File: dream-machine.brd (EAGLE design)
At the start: 17.8 x 21.6 mm, 8 parts, among them J1 AVR_SPI_PRG_62X3_LOCK, SW1 Now, U1 ATTINY13SOIC

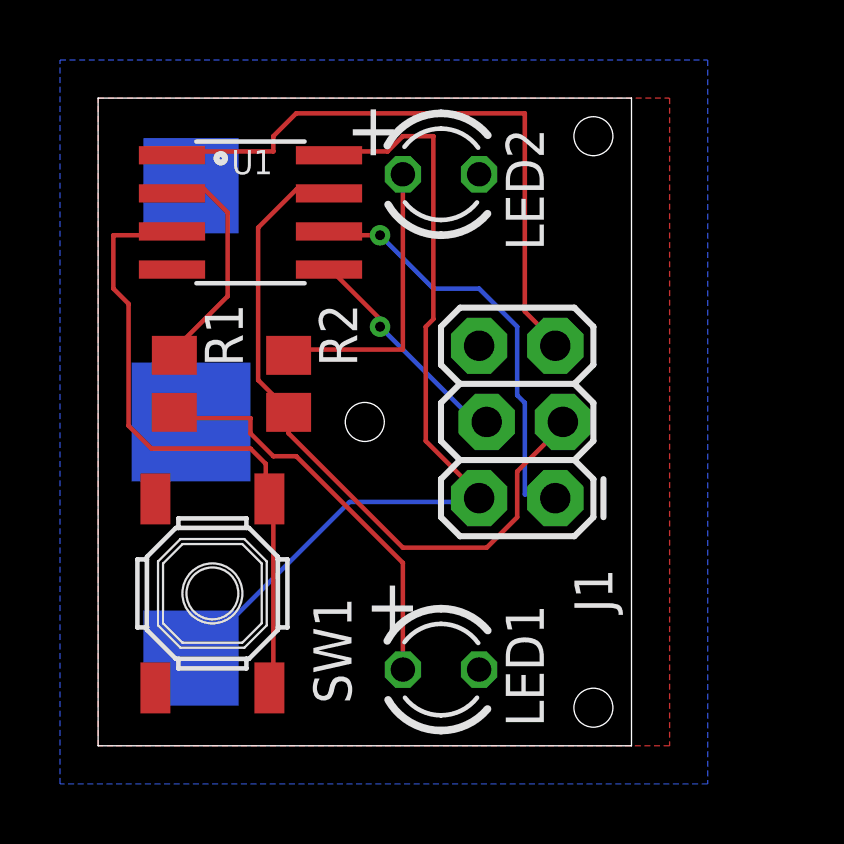
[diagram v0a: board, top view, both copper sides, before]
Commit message: Added power jumper. Fixed orientation of battery holder.
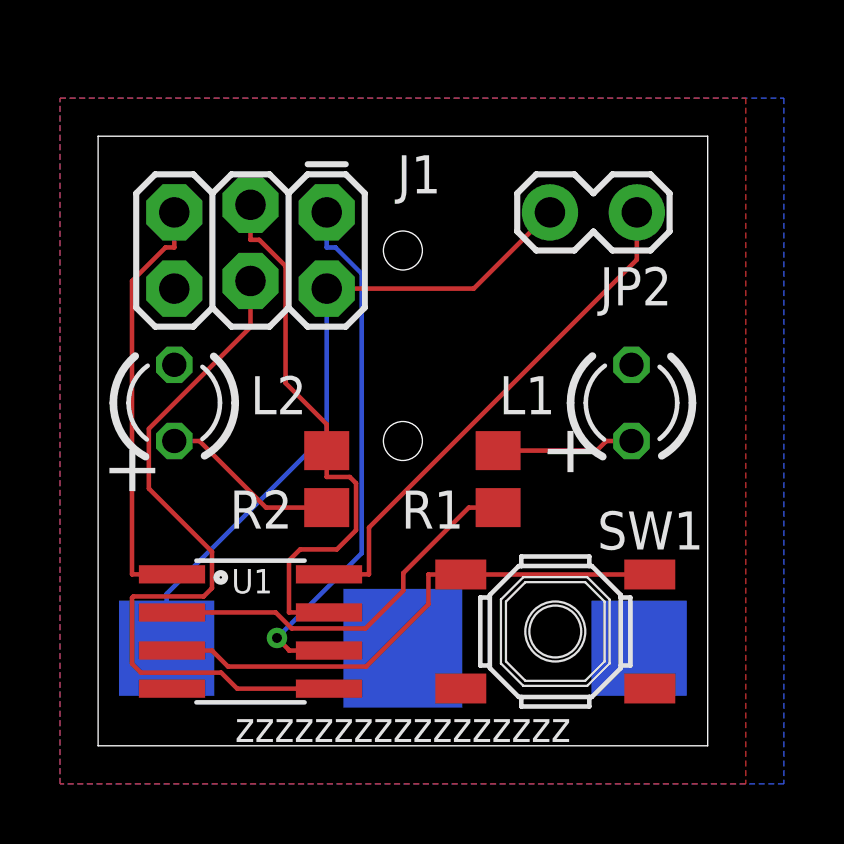
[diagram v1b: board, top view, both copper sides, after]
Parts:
- removed LED1: LEFT, dp_devices:LED-3MM
- removed LED2: RIGHT, dp_devices:LED-3MM
- added JP2: POWER, SparkFun:1X02_LOCK
- added L1: LEFT, dp_devices:LED-3MM
- added L2: RIGHT, dp_devices:LED-3MM
- moved U1 14.0 mm to (5.08, 3.81)
- moved J1 12.2 mm to (7.62, 17.8), turned to 180 degrees
- moved SW1 11.5 mm to (15.2, 3.81), turned to 0 degrees
- moved R1 11.3 mm to (13.3, 8.89), turned to 90 degrees
- moved BAT1 10.3 mm to (10.2, 3.25), turned to 180 degrees
- moved R2 3.42 mm to (7.62, 8.89), turned to 270 degrees
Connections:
- new net VCC-POWER: JP2.1, U1.8
- net GND: now also L1.K, L2.K; no longer LED1.K, LED2.K
- net L1-R: now also L1.A; no longer LED1.A
- net L2-R: now also L2.A; no longer LED2.A
- net VCC: now also JP2.2; no longer U1.8
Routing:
- net VCC-POWER: track 0.00 -> 17.1 mm
- net MOSI: track 7.57 -> 24.4 mm, vias 1 -> 0
- net L1-R: track 13.7 -> 4.58 mm
- net /RESET: track 20.8 -> 14.2 mm
- net VCC: track 28.5 -> 22.7 mm
- net PB3: track 7.74 -> 13.1 mm
- net PB2/SCK: track 23.7 -> 18.6 mm
- net L2-R: track 9.85 -> 6.00 mm
- net MISO: track 14.4 -> 17.9 mm
- net PB4: track 21.3 -> 18.0 mm
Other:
- board size 17.8 x 21.6 mm -> 20.3 x 20.3 mm
- board text added: "Dream"
- board text added: "zzzzzzzzzzzzzzzzz"
- board text removed: "LUCID"
